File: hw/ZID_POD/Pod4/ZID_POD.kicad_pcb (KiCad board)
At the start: 2 copper layers, 52.8 x 19.3 mm, 2 parts, among them J1 Z80-POD (4)

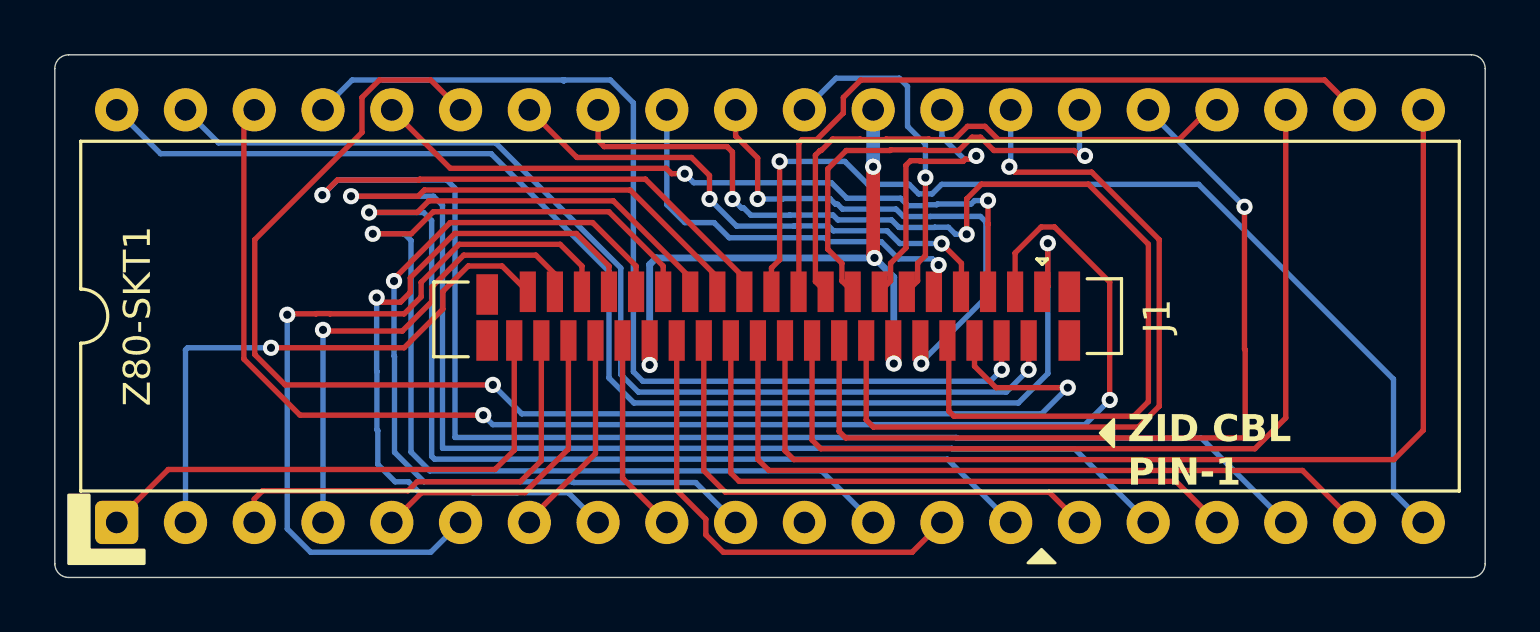
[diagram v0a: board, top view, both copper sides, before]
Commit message: PCB: Ready to order - ZID, POD1, POD2, POD3, POD4, ExpBP
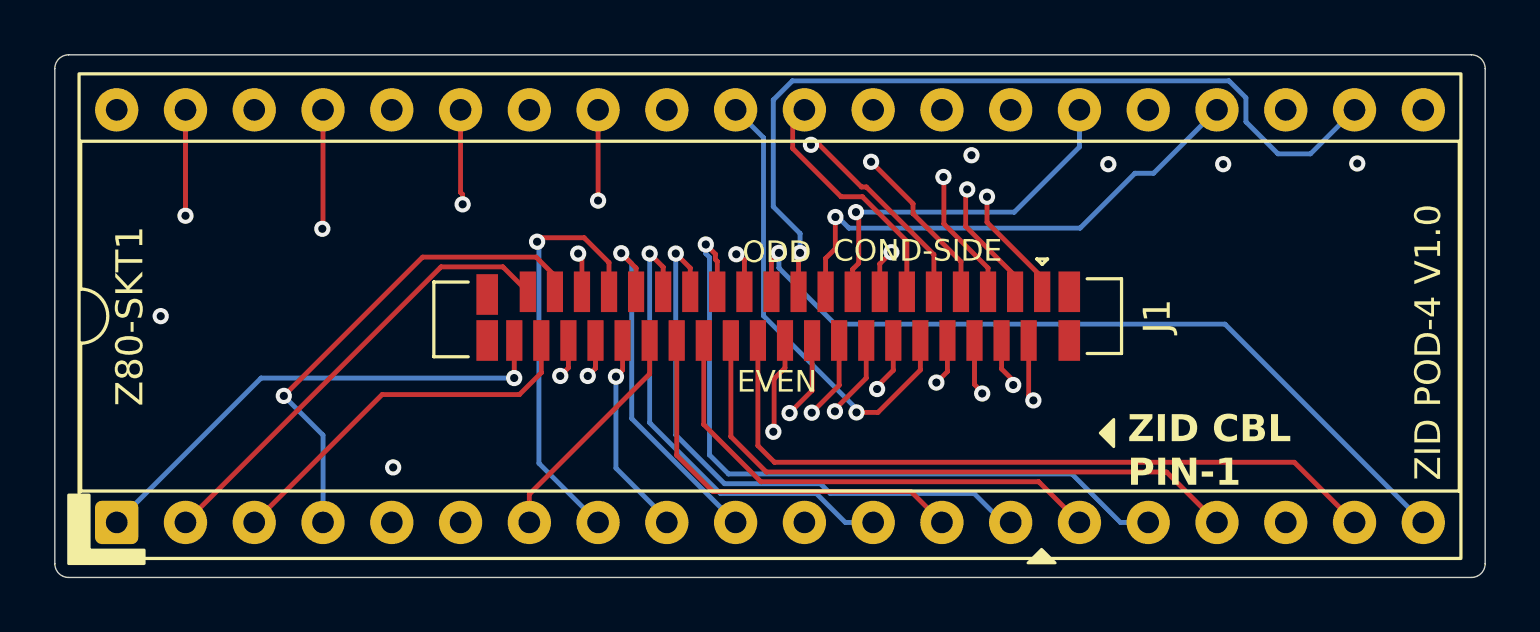
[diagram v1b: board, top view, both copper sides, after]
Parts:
- J1: value Z80-POD (4) -> FFC/FPC-40 Socket
- Z80-SKT1: footprint Package_DIP:DIP-40_W15.24mm -> Package_DIP:DIP-40_W15.24mm_Socket
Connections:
- J1 pad 12: /GND -> /A15
- J1 pad 30: /GND -> /D4
- J1 pad 34: /D4 -> /GND
- J1 pad 36: /A15 -> /GND
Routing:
- net /HALT-: track 63.8 -> 30.1 mm
- net /INT-: track 54.7 -> 27.0 mm
- net /D0: track 46.8 -> 21.8 mm
- net /D2: track 40.3 -> 17.6 mm
- net /A5: track 51.6 -> 29.1 mm
- net /A3: track 42.4 -> 21.3 mm
- net /A8: track 52.7 -> 31.6 mm, vias 2 -> 1
- net /GND: track 23.6 -> 2.86 mm, vias 4 -> 7
- net /D6: track 31.5 -> 13.3 mm
- net /CLK: track 28.7 -> 13.2 mm
- net /A15: track 11.7 -> 24.2 mm, vias 0 -> 2
- net /D3: track 26.7 -> 15.5 mm
- net /A10: track 48.3 -> 37.6 mm
- net /IORQ-: track 37.0 -> 29.8 mm
- net /M1-: track 29.1 -> 23.8 mm
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- added copper zone on In1.Cu, net /GND
- added copper zone on In2.Cu, net /GND
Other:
- copper layers 2 -> 4
- board text added: "ZID POD-4 V1.0"
